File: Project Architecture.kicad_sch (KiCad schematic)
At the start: 0 parts

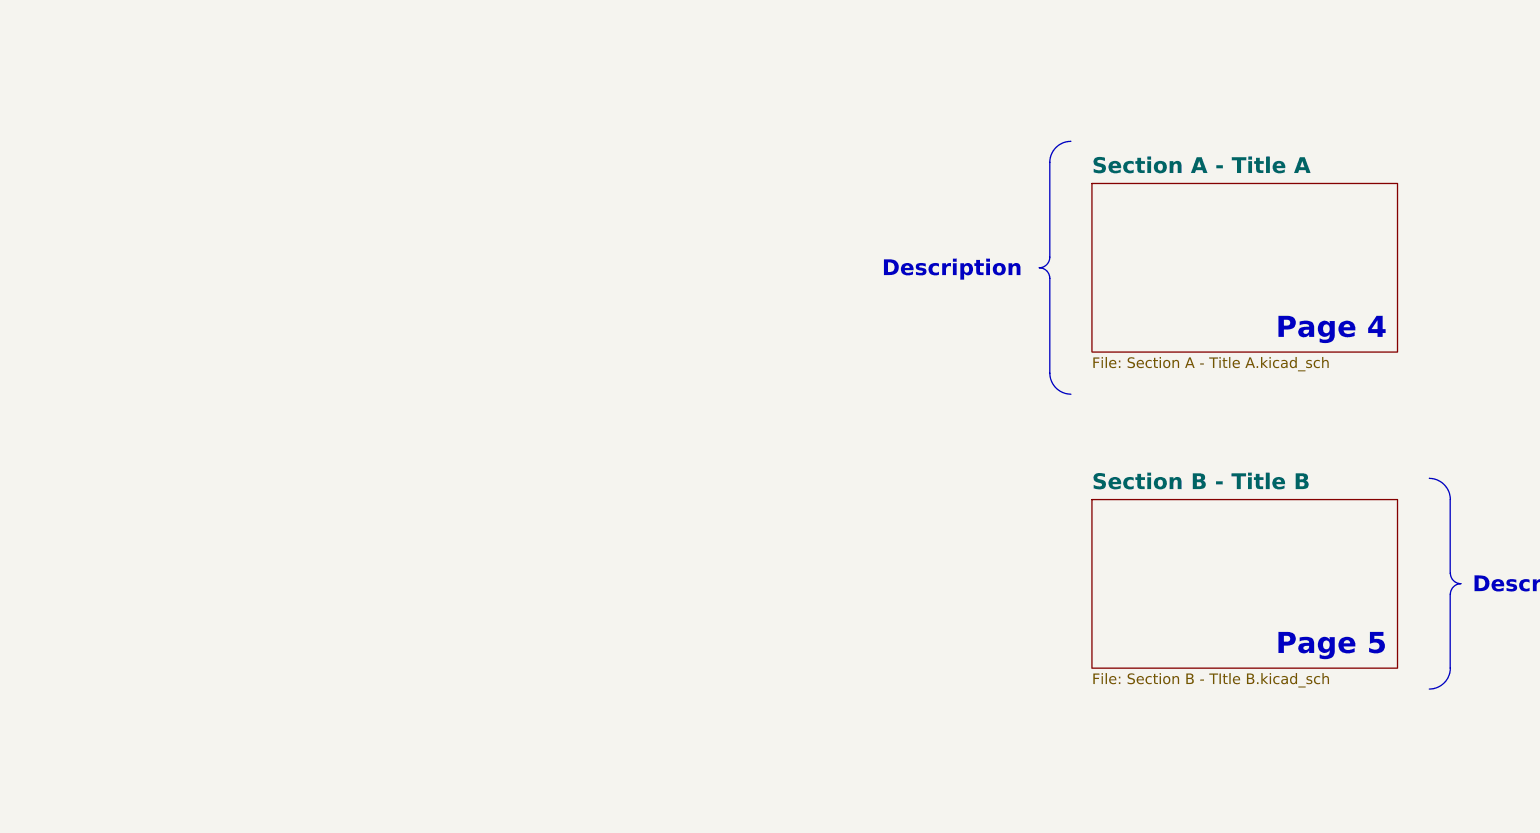
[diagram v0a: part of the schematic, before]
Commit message: [24/06/2026] Block Diagram Update
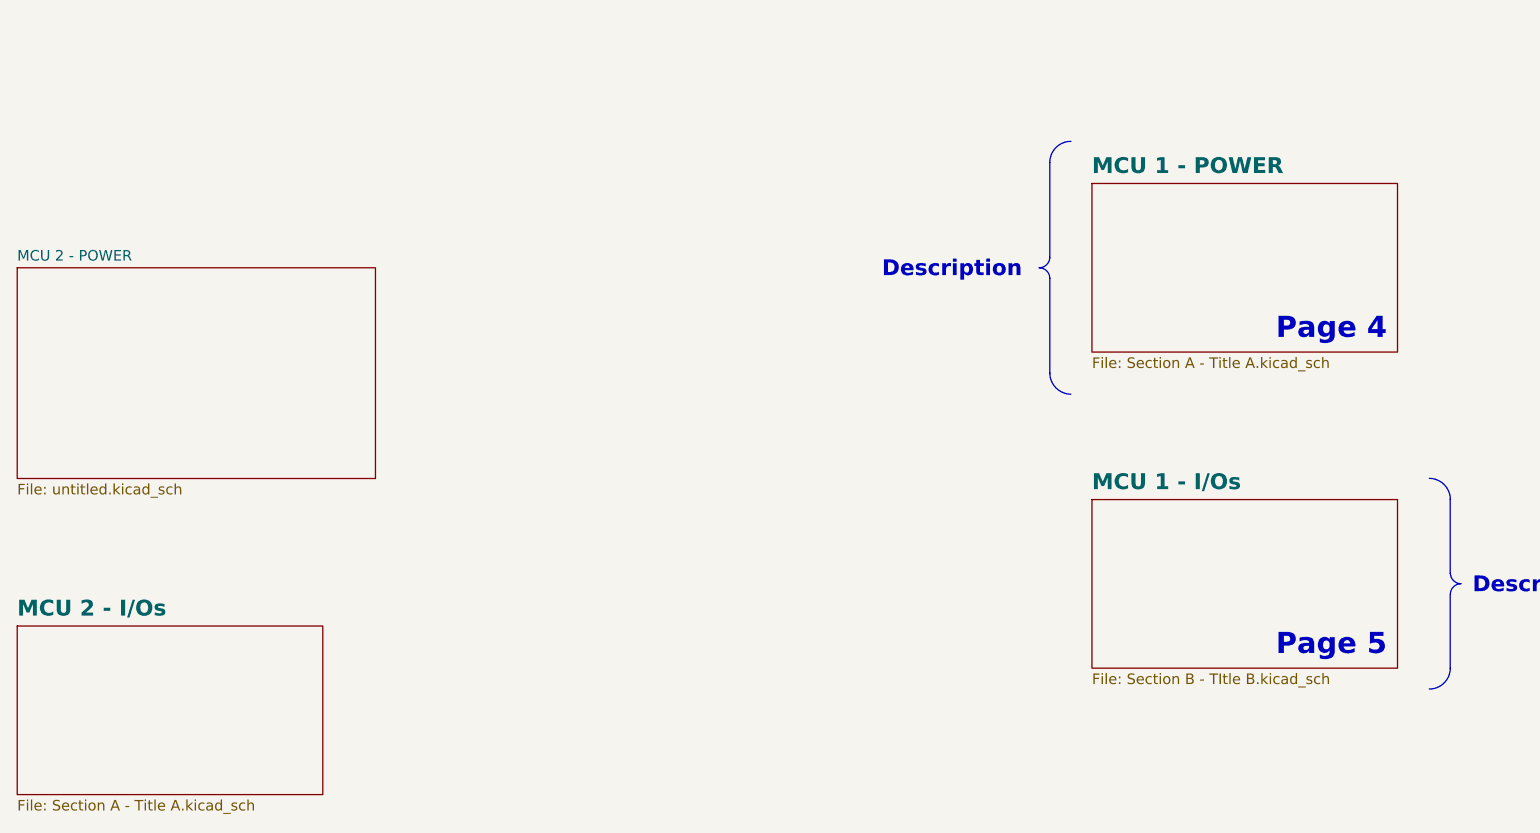
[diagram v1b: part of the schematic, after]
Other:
- sheet Section A - Title A renamed MCU 1 - POWER
- sheet Section B - Title B renamed MCU 1 - I/Os
- added sheet MCU 2 - I/Os (Section A - Title A.kicad_sch)
- added sheet MCU 2 - POWER (untitled.kicad_sch)
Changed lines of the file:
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@@
+	)
+	(sheet
+		(at 60.96 86.36)
+		(size 43.18 25.4)
+		(exclude_from_sim no)
+		(in_bom yes)
+		(on_board yes)
+		(dnp no)
+		(fields_autoplaced yes)
+		(stroke
+			(width 0.1524)
+			(type solid)
+		)
+		(fill
+			(color 0 0 0 0.0000)
+		)
+		(property "Sheetname" "MCU 2 - POWER"
+			(at 60.96 85.6484 0)
+			(effects
+				(font
+					(size 1.27 1.27)
+				)
+				(justify left bottom)
+			)
+		)
+		(property "Sheetfile" "untitled.kicad_sch"
+			(at 60.96 112.3446 0)
+			(effects
+				(font
+					(size 1.27 1.27)
+				)
+				(justify left top)
+			)
+		)
+		(instances
+			(project "Master_Hand_Kicad"
+				(path "/f9e05184-c88b-4a88-ae9c-ab2bdb32be7c/c5103ceb-5325-4a84-a025-9638a412984e"
+					(page "6")
+				)
+			)
+		)
+	)
+	(sheet
+		(at 60.96 129.54)
+		(size 36.83 20.32)
+		(exclude_from_sim no)
+		(in_bom yes)
+		(on_board yes)
+		(dnp no)
+		(fields_autoplaced yes)
+		(stroke
+			(width 0.1524)
+			(type solid)
+		)
+		(fill
+			(color 128 255 128 0.5000)
+		)
+		(property "Sheetname" "MCU 2 - I/Os"
+			(at 60.96 128.5109 0)
+			(effects
+				(font
+					(size 1.905 1.905)
+					(bold yes)
+				)
+				(justify left bottom)
+			)
+		)
+		(property "Sheetfile" "Section A - Title A.kicad_sch"
+			(at 60.96 150.4446 0)
+			(effects
+				(font
+					(face "Arial")
+					(size 1.27 1.27)
+				)
+				(justify left top)
+			)
+		)
+		(instances
+			(project "Master_Hand_Kicad"
+				(path "/f9e05184-c88b-4a88-ae9c-ab2bdb32be7c/c5103ceb-5325-4a84-a025-9638a412984e"
+					(page "7")
+				)
+			)
+		)
 	)
 	(sheet
@@
 			(color 255 200 0 0.5020)
 		)
-		(property "Sheetname" "Section B - Title B"
+		(property "Sheetname" "MCU 1 - I/Os"
 			(at 190.5 113.2709 0)
 			(effects
@@
 			(color 128 255 128 0.5000)
 		)
-		(property "Sheetname" "Section A - Title A"
+		(property "Sheetname" "MCU 1 - POWER"
 			(at 190.5 75.1709 0)
 			(effects

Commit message: [25/06/2026][MCU-POWER] Update
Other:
- sheet MCU 1 - I/Os renamed MCU - I/Os
- sheet MCU 1 - POWER renamed MCU - POWER
- removed sheet MCU 2 - I/Os
- removed sheet MCU 2 - POWER
- sheet MCU - POWER: file Section A - Title A.kicad_sch -> MCU - POWER.kicad_sch
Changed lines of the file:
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@@
-	)
-	(sheet
-		(at 60.96 86.36)
-		(size 43.18 25.4)
-		(exclude_from_sim no)
-		(in_bom yes)
-		(on_board yes)
-		(dnp no)
-		(fields_autoplaced yes)
-		(stroke
-			(width 0.1524)
-			(type solid)
-		)
-		(fill
-			(color 0 0 0 0.0000)
-		)
-		(property "Sheetname" "MCU 2 - POWER"
-			(at 60.96 85.6484 0)
-			(effects
-				(font
-					(size 1.27 1.27)
-				)
-				(justify left bottom)
-			)
-		)
-		(property "Sheetfile" "untitled.kicad_sch"
-			(at 60.96 112.3446 0)
-			(effects
-				(font
-					(size 1.27 1.27)
-				)
-				(justify left top)
-			)
-		)
-		(instances
-			(project "Master_Hand_Kicad"
-				(path "/f9e05184-c88b-4a88-ae9c-ab2bdb32be7c/c5103ceb-5325-4a84-a025-9638a412984e"
-					(page "6")
-				)
-			)
-		)
-	)
-	(sheet
-		(at 60.96 129.54)
-		(size 36.83 20.32)
-		(exclude_from_sim no)
-		(in_bom yes)
-		(on_board yes)
-		(dnp no)
-		(fields_autoplaced yes)
-		(stroke
-			(width 0.1524)
-			(type solid)
-		)
-		(fill
-			(color 128 255 128 0.5000)
-		)
-		(property "Sheetname" "MCU 2 - I/Os"
-			(at 60.96 128.5109 0)
-			(effects
-				(font
-					(size 1.905 1.905)
-					(bold yes)
-				)
-				(justify left bottom)
-			)
-		)
-		(property "Sheetfile" "Section A - Title A.kicad_sch"
-			(at 60.96 150.4446 0)
-			(effects
-				(font
-					(face "Arial")
-					(size 1.27 1.27)
-				)
-				(justify left top)
-			)
-		)
-		(instances
-			(project "Master_Hand_Kicad"
-				(path "/f9e05184-c88b-4a88-ae9c-ab2bdb32be7c/c5103ceb-5325-4a84-a025-9638a412984e"
-					(page "7")
-				)
-			)
-		)
 	)
 	(sheet
@@
 			(color 255 200 0 0.5020)
 		)
-		(property "Sheetname" "MCU 1 - I/Os"
+		(property "Sheetname" "MCU - I/Os"
 			(at 190.5 113.2709 0)
 			(effects
@@
 			(color 128 255 128 0.5000)
 		)
-		(property "Sheetname" "MCU 1 - POWER"
+		(property "Sheetname" "MCU - POWER"
 			(at 190.5 75.1709 0)
 			(effects
@@
 			)
 		)
-		(property "Sheetfile" "Section A - Title A.kicad_sch"
+		(property "Sheetfile" "MCU - POWER.kicad_sch"
 			(at 190.5 97.1046 0)
 			(effects

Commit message: [25/06/2025][MCU - IOs] Update
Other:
- sheet MCU - I/Os renamed MCU - IOs
- added sheet Interface - FD-CAN (Interface - FD-CAN.kicad_sch)
- added sheet Interface - FD-CAN1 (Interface - FD-CAN.kicad_sch)
- added sheet Interface - Interconnects (Interface - Interconnects.kicad_sch)
- added sheet Interface - RS-485 (Interface - RS-422.kicad_sch)
- added sheet Misc - Board Version, DAC (Misc - Board Version DAC.kicad_sch)
- added sheet Misc - Holes, Fiducials (Misc - Holes Fiducials.kicad_sch)
- added sheet Motor Control - Top Level (Motor Control - Top Level.kicad_sch)
- added sheet Power - Connectors (Power - Connectors.kicad_sch)
- added sheet Power - Generation (Power - Generation.kicad_sch)
- added sheet Sensing - Battery (Sensing - Battery.kicad_sch)
- added sheet Sensing - Position (Sensing - Position.kicad_sch)
- added sheet Sensing - Temperature (Sensing - Temperature.kicad_sch)
- added sheet User - LED Indicators (User - LED Indicators.kicad_sch)
- sheet MCU - IOs: file Section B - TItle B.kicad_sch -> MCU - IOs.kicad_sch

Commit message: [26/06/2026][MCU - IOs] Update
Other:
- removed sheet Interface - FD-CAN
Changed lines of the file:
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@@
-	)
-	(sheet
-		(at 140.97 238.76)
-		(size 31.75 12.7)
-		(exclude_from_sim no)
-		(in_bom yes)
-		(on_board yes)
-		(dnp no)
-		(fields_autoplaced yes)
-		(stroke
-			(width 0.1524)
-			(type solid)
-		)
-		(fill
-			(color 255 150 255 0.5000)
-		)
-		(property "Sheetname" "Interface - FD-CAN"
-			(at 140.97 237.7309 0)
-			(effects
-				(font
-					(size 1.905 1.905)
-					(bold yes)
-				)
-				(justify left bottom)
-			)
-		)
-		(property "Sheetfile" "Interface - FD-CAN.kicad_sch"
-			(at 140.97 252.0446 0)
-			(effects
-				(font
-					(face "Arial")
-					(size 1.27 1.27)
-				)
-				(justify left top)
-			)
-		)
-		(pin "{FDCAN_TTL}" bidirectional
-			(at 172.72 242.57 0)
-			(effects
-				(font
-					(size 1.27 1.27)
-					(thickness 0.254)
-					(bold yes)
-				)
-				(justify right)
-			)
-		)
-		(pin "{FDCAN}" bidirectional
-			(at 140.97 242.57 180)
-			(effects
-				(font
-					(size 1.27 1.27)
-					(thickness 0.254)
-					(bold yes)
-				)
-				(justify left)
-			)
-		)
-		(instances
-			(project "Master_Hand_Kicad"
-				(path "/f9e05184-c88b-4a88-ae9c-ab2bdb32be7c/c5103ceb-5325-4a84-a025-9638a412984e"
-					(page "8")
-				)
-			)
-		)
 	)
 	(sheet
